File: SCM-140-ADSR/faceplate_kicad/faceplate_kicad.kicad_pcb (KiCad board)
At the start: 2 copper layers, 50.5 x 128.5 mm, 14 parts

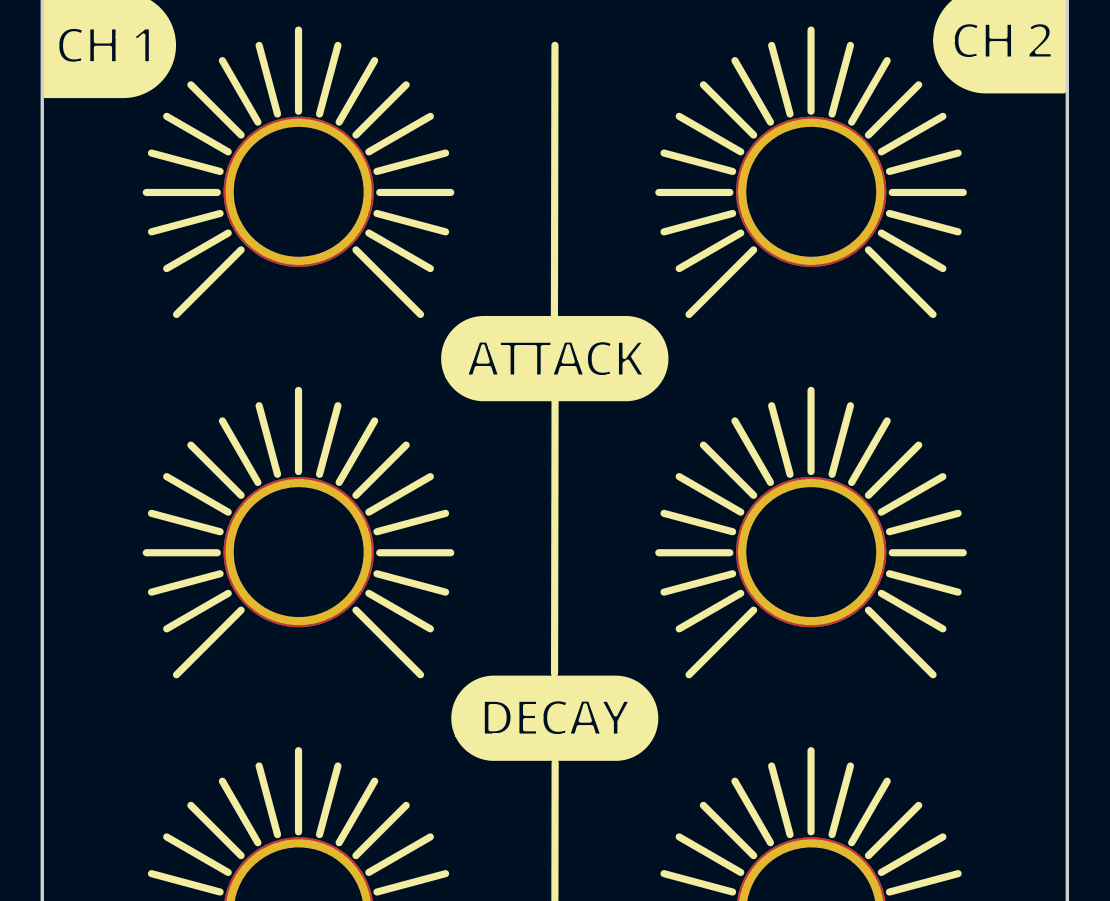
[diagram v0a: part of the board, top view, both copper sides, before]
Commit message: Add M3 mounting holes for mechanical stability
In case non-threaded potentiometers are used
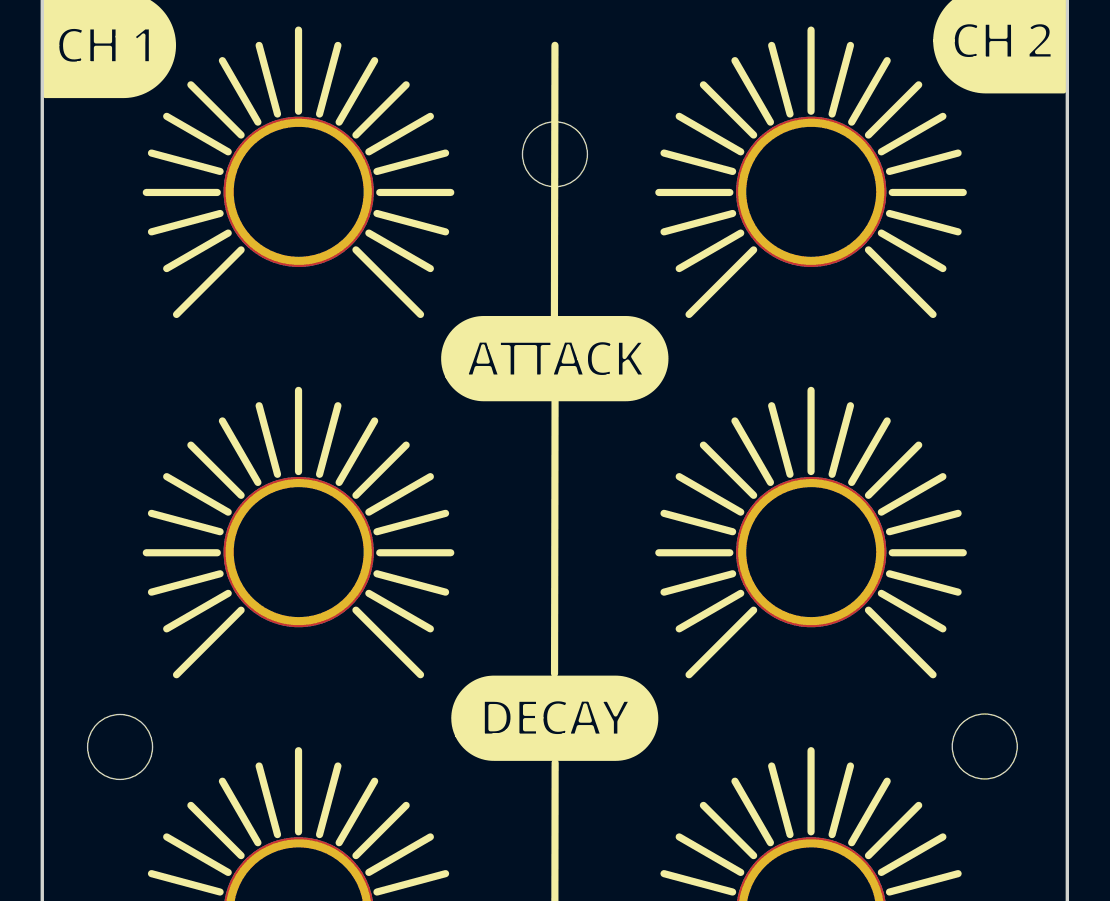
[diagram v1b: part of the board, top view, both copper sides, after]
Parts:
- added REF**: MountingHole_3.2mm_M3, MountingHole:MountingHole_3.2mm_M3, F.Cu at (156.8, 73.2)
- added REF**: MountingHole_3.2mm_M3, MountingHole:MountingHole_3.2mm_M3, F.Cu at (114.2, 73.2)
- added REF**: MountingHole_3.2mm_M3, MountingHole:MountingHole_3.2mm_M3, F.Cu at (135.7, 44.0)
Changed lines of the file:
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@@
     (pad "1" thru_hole circle (at 0 0) (size 6.8 6.8) (drill 6.4) (layers *.Cu *.Mask))
+  )
+  (footprint "MountingHole:MountingHole_3.2mm_M3" (layer "F.Cu")
+    (at 156.85 73.176278)
+    (descr "Mounting Hole 3.2mm, no annular, M3")
+    (tags "mounting hole 3.2mm no annular m3")
+    (attr exclude_from_pos_files exclude_from_bom)
+    (fp_text reference "REF**" (at 0 -4.2) (layer "F.SilkS") hide
+      (effects (font (size 1 1) (thickness 0.15)))
+    )
+    (fp_text value "MountingHole_3.2mm_M3" (at 0 4.2) (layer "F.Fab")
+      (effects (font (size 1 1) (thickness 0.15)))
+    )
+    (fp_text user "${REFERENCE}" (at 0 0) (layer "F.Fab")
+      (effects (font (size 1 1) (thickness 0.15)))
+    )
+    (fp_circle (center 0 0) (end 3.2 0) (layer "Cmts.User") (width 0.15) (fill none))
+    (fp_circle (center 0 0) (end 3.45 0) (layer "F.CrtYd") (width 0.05) (fill none))
+    (pad "" np_thru_hole circle (at 0 0) (size 3.2 3.2) (drill 3.2) (layers *.Cu *.Mask))
   )
   (footprint "Library:MountingHole_7.2mm_Pad_TopBottom" (layer "F.Cu")
@@
     (pad "1" connect circle (at 0 0) (size 6.4 6.4) (layers "B.Cu" "B.Mask"))
   )
+  (footprint "MountingHole:MountingHole_3.2mm_M3" (layer "F.Cu")
+    (at 114.25 73.2)
+    (descr "Mounting Hole 3.2mm, no annular, M3")
+    (tags "mounting hole 3.2mm no annular m3")
+    (attr exclude_from_pos_files exclude_from_bom)
+    (fp_text reference "REF**" (at 0 -4.2) (layer "F.SilkS") hide
+      (effects (font (size 1 1) (thickness 0.15)))
+    )
+    (fp_text value "MountingHole_3.2mm_M3" (at 0 4.2) (layer "F.Fab")
+      (effects (font (size 1 1) (thickness 0.15)))
+    )
+    (fp_text user "${REFERENCE}" (at 0 0) (layer "F.Fab")
+      (effects (font (size 1 1) (thickness 0.15)))
+    )
+    (fp_circle (center 0 0) (end 3.2 0) (layer "Cmts.User") (width 0.15) (fill none))
+    (fp_circle (center 0 0) (end 3.45 0) (layer "F.CrtYd") (width 0.05) (fill none))
+    (pad "" np_thru_hole circle (at 0 0) (size 3.2 3.2) (drill 3.2) (layers *.Cu *.Mask))
+  )
   (footprint "Library:MountingHole_7.2mm_Pad_TopBottom" (layer "F.Cu")
     (at 148.3 45.85)
@@
     (pad "1" thru_hole circle (at 0 0) (size 7.2 7.2) (drill 6.4) (layers *.Cu *.Mask))
   )
+  (footprint "MountingHole:MountingHole_3.2mm_M3" (layer "F.Cu")
+    (at 135.675 44)
+    (descr "Mounting Hole 3.2mm, no annular, M3")
+    (tags "mounting hole 3.2mm no annular m3")
+    (attr exclude_from_pos_files exclude_from_bom)
+    (fp_text reference "REF**" (at 0 -4.2) (layer "F.SilkS") hide
+      (effects (font (size 1 1) (thickness 0.15)))
+    )
+    (fp_text value "MountingHole_3.2mm_M3" (at 0 4.2) (layer "F.Fab")
+      (effects (font (size 1 1) (thickness 0.15)))
+    )
+    (fp_text user "${REFERENCE}" (at 0 0) (layer "F.Fab")
+      (effects (font (size 1 1) (thickness 0.15)))
+    )
+    (fp_circle (center 0 0) (end 3.2 0) (layer "Cmts.User") (width 0.15) (fill none))
+    (fp_circle (center 0 0) (end 3.45 0) (layer "F.CrtYd") (width 0.05) (fill none))
+    (pad "" np_thru_hole circle (at 0 0) (size 3.2 3.2) (drill 3.2) (layers *.Cu *.Mask))
+  )
   (footprint "Library:MountingHole_7.2mm_Pad_TopBottom" (layer "F.Cu")
